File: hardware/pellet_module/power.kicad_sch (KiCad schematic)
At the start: 18 parts, among them J19 Barrel_Jack, U8 MIC5219-3.3YM5, U9 TPS565208

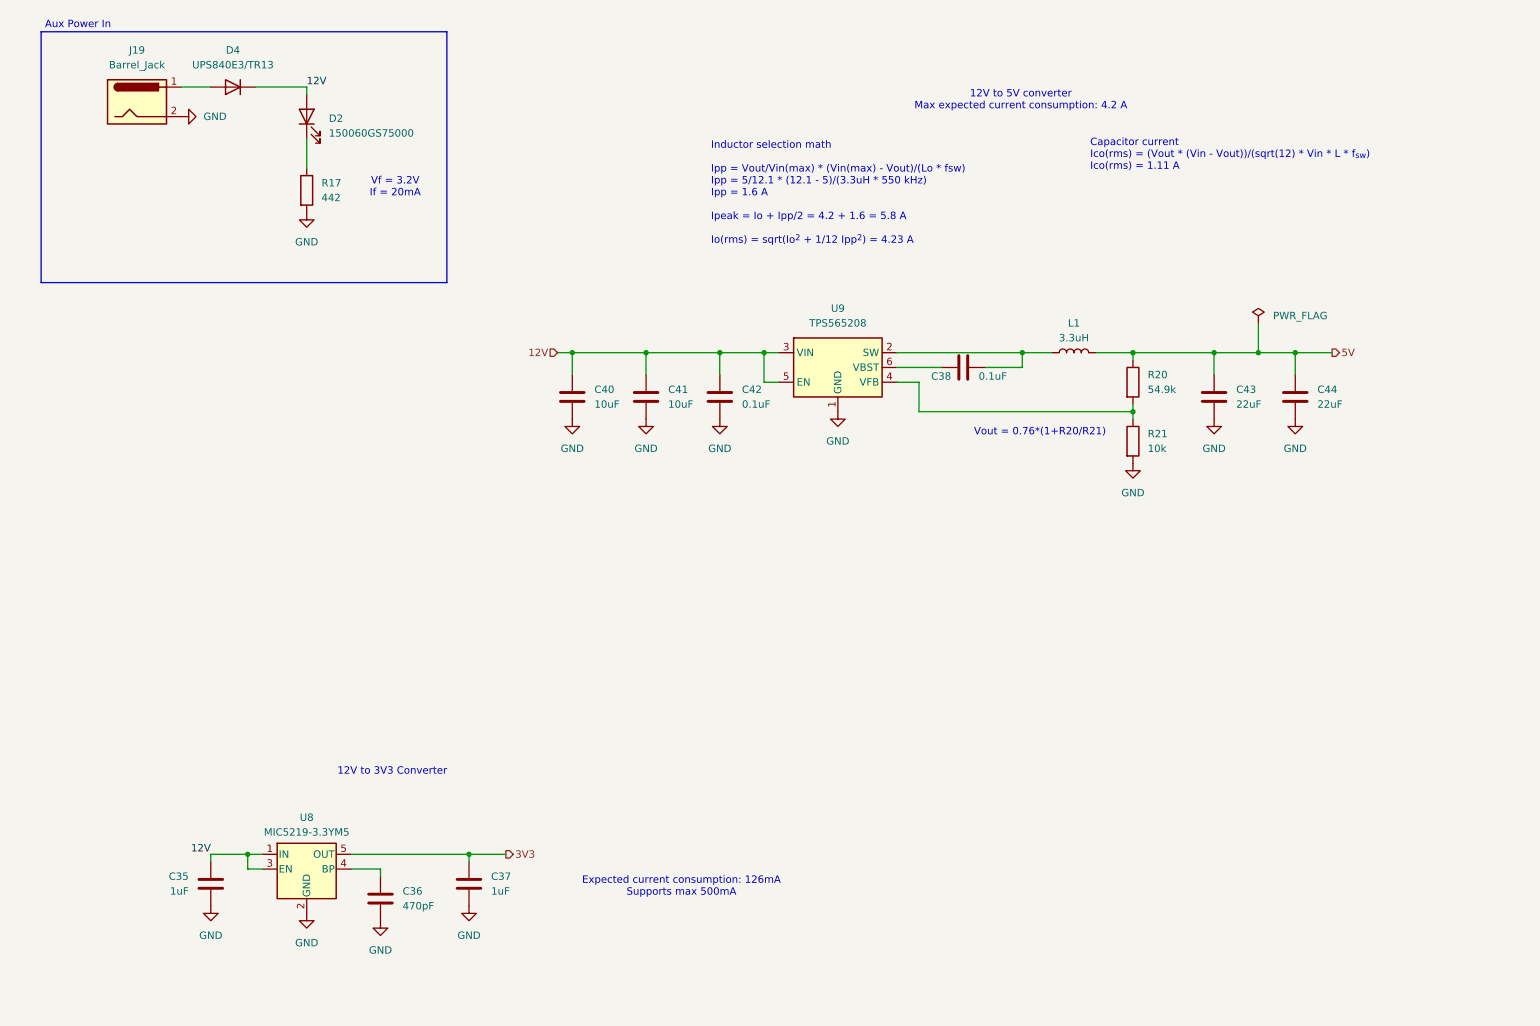
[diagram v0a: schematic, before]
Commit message: add test points, mpns, datasheets
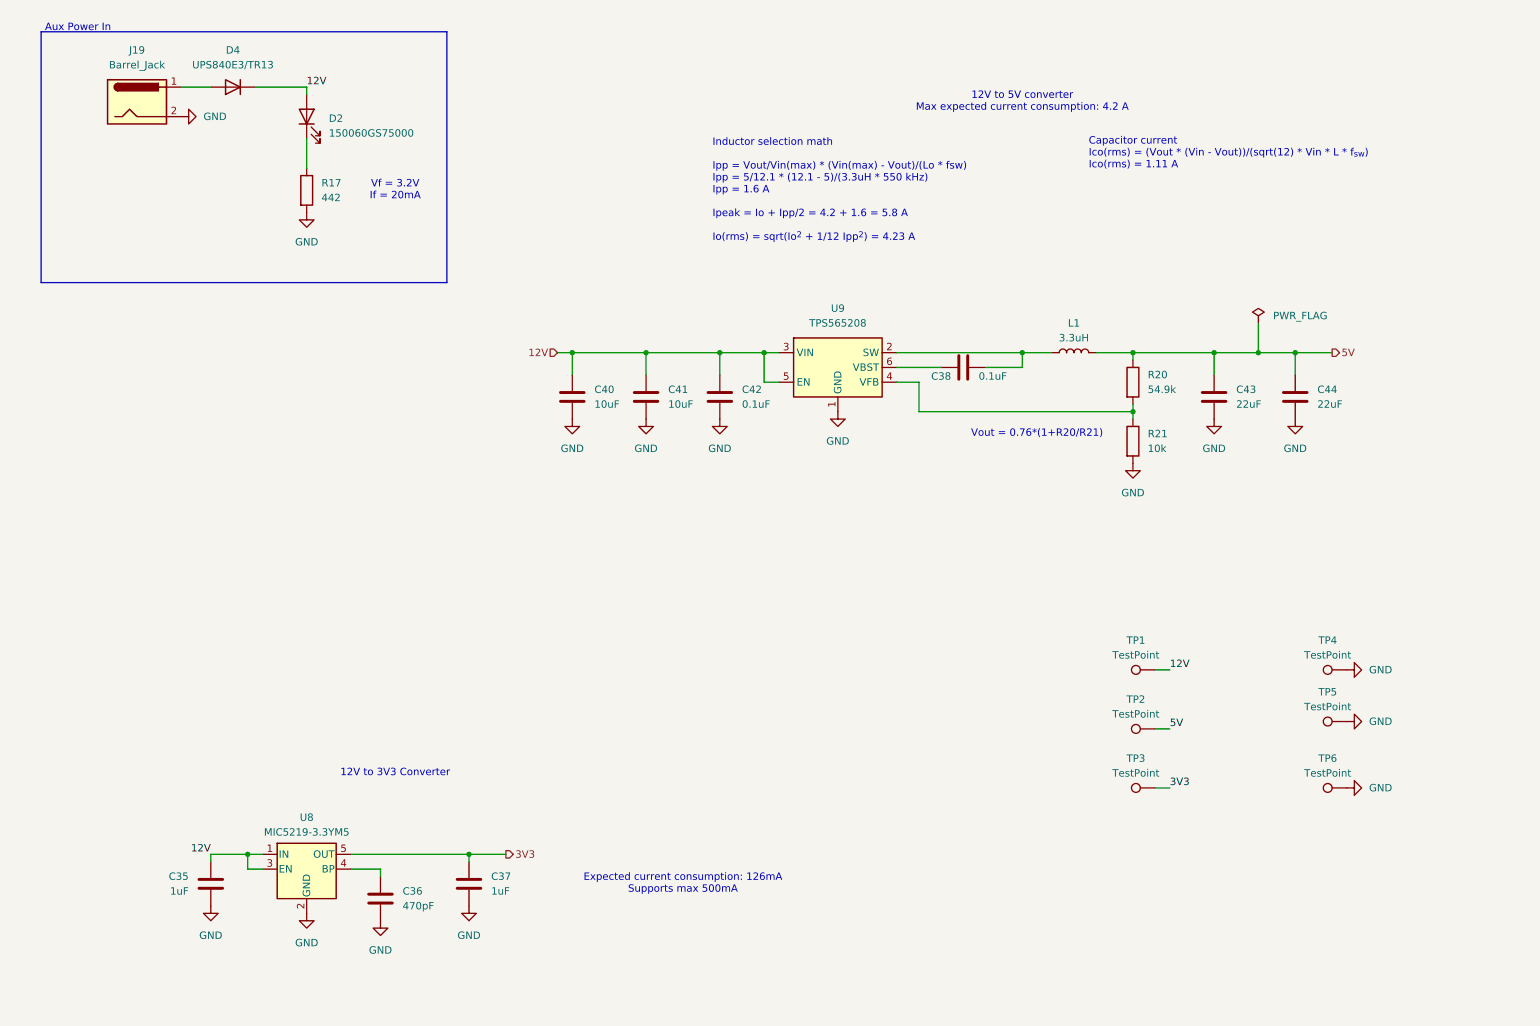
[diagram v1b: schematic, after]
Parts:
- added TP1, TP2, TP3, TP4, TP5, TP6: TestPoint, symbol Connector:TestPoint
- C35, C37: footprint (none) -> Capacitor_SMD:C_0603_1608Metric; MPN (none) -> CC0603KRX7R7BB105
- C36: footprint (none) -> Capacitor_SMD:C_0603_1608Metric; MPN (none) -> CL10C471JB8NNNC
- C38, C42: footprint (none) -> Capacitor_SMD:C_0603_1608Metric; MPN (none) -> CC0603ZRY5V9BB104
- C40, C41: footprint (none) -> Capacitor_SMD:C_0603_1608Metric; MPN (none) -> GRM188R61E106KA73D
- C43, C44: footprint (none) -> Capacitor_SMD:C_0603_1608Metric; MPN (none) -> GRM188R61A226ME15D
- D2: footprint (none) -> Diode_SMD:D_0603_1608Metric; MPN (none) -> 150060GS75000
- D4: footprint (none) -> Diode_SMD:D_Powermite3; MPN (none) -> UPS840E3/TR13
- J19: MPN (none) -> DCJ200-10-A-K1-K
- L1: MPN (none) -> VLS6045EX-3R3N
- R17: MPN (none) -> RC0603FR-07442RL
- R20: MPN (none) -> RC0603FR-0754K9L
- R21: MPN (none) -> RC0603FR-0710KL
- U8: MPN (none) -> MIC5219-3.3YM5
- U9: MPN (none) -> TPS565208
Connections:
- net 12V: now also TP1.1
- net 3V3: now also TP3.1
- net 5V: now also TP2.1
- net GND: now also TP4.1, TP5.1, TP6.1

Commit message: add titles, ESD protection, make changes requested by Ryan
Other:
- company: (none) -> Christie Lab, CU-Anschutz
- title: (none) -> Autotrainer Pellet Module - Power
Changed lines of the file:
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@@
 	(generator_version "8.0")
 	(paper "A4")
+	(title_block
+		(title "Autotrainer Pellet Module - Power")
+		(date "2024-07-09")
+		(rev "v1.0")
+		(company "Christie Lab, CU-Anschutz")
+		(comment 1 "Prepared by LeafLabs, LLC")
+	)
 	(junction
 		(at 134.62 73.66)

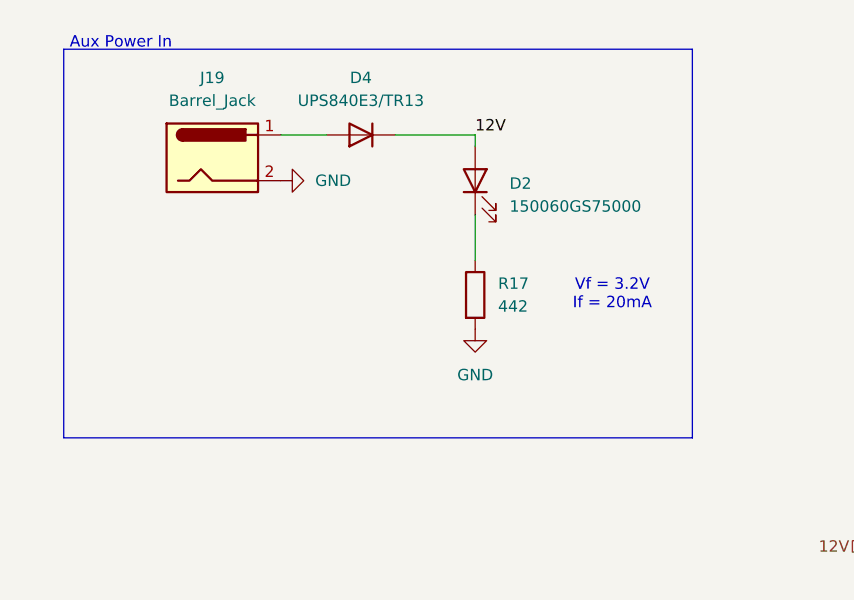
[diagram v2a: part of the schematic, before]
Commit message: * Add footprints for every part * Change power LED from 20mA to 4mA * Edit symbols to match footprints (EPAD -> pin numbers) to eliminate errors on import to pcbnew
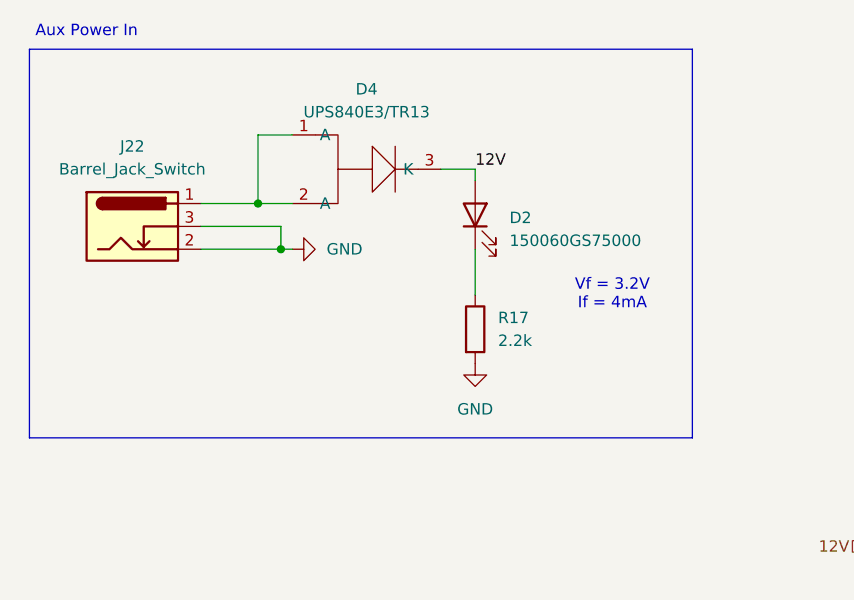
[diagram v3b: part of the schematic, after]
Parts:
- removed J19: Barrel_Jack, symbol Connector:Barrel_Jack
- added J22: Barrel_Jack_Switch, Connector_BarrelJack:BarrelJack_GCT_DCJ200-10-A_Horizontal, symbol Connector:Barrel_Jack_Switch
- D4: symbol Device:D -> Leaf_Diode:Diode_123
- L1: footprint (none) -> Inductor_SMD:L_TDK_VLS6045EX_VLS6045AF
- R17: value 442 -> 2.2k; footprint (none) -> Resistor_SMD:R_0603_1608Metric; MPN RC0603FR-07442RL -> (none)
- R20, R21: footprint (none) -> Resistor_SMD:R_0603_1608Metric
- TP1, TP2, TP3, TP4, TP5, TP6: footprint (none) -> TestPoint:TestPoint_Pad_1.0x1.0mm
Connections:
- net 12V: now also D4.3 (K); no longer D4.1 (K)
- net GND: now also J22.2, J22.3
- net at D4.2 (A): now also D4.1 (A), J22.1
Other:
- note added: "Vf = 3.2V If = 4mA"
- note removed: "Vf = 3.2V If = 20mA"
- moved on the sheet: D2, R17

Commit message: update mechanicals based on dan's comments
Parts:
- D4: footprint Diode_SMD:D_Powermite3 -> Leaf_Diode:POWERMITE3_MCH
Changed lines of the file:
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@@
 			)
 		)
-		(property "Footprint" "Diode_SMD:D_Powermite3"
+		(property "Footprint" "Leaf_Diode:POWERMITE3_MCH"
 			(at 52.07 29.21 0)
 			(effects

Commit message: Releases layout for pellet, magnet, and Jetson breakout boards.
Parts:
- removed U8: MIC5219-3.3YM5, Package_TO_SOT_SMD:SOT-23-5, symbol Regulator_Linear:MIC5219-3.3YM5
- added C49: 10uF, Capacitor_SMD:C_0603_1608Metric, symbol Device:C
- added L2: 3.3uH, Leaf_Inductor:L_Taiyo_Yuden_MAMK, symbol Device:L
- added R27: 33.2k, Resistor_SMD:R_0603_1608Metric, symbol Device:R
- added R28: 10k, Resistor_SMD:R_0603_1608Metric, symbol Device:R
- added U8: TPS561201, Package_TO_SOT_SMD:SOT-23-6, symbol Leaf_Regulator:TPS56120x
- C35: value 1uF -> 0.1uF; LCSC (none) -> C14663; MPN CC0603KRX7R7BB105 -> CC0603KRX7R9BB104
- C36: value 470pF -> 22uF; LCSC (none) -> C59461; MPN CL10C471JB8NNNC -> CL10A226MQ8NRNC
- C37: value 1uF -> 22uF; LCSC (none) -> C59461; MPN CC0603KRX7R7BB105 -> CL10A226MQ8NRNC
- C38, C42: LCSC (none) -> C14663; MPN CC0603ZRY5V9BB104 -> CC0603KRX7R9BB104
- C40, C41: LCSC (none) -> C96446; MPN GRM188R61E106KA73D -> CL10A106MA8NRNC
- C43, C44: LCSC (none) -> C59461; MPN GRM188R61A226ME15D -> CL10A226MQ8NRNC
- D2: LCSC (none) -> C5252984
- D4: LCSC (none) -> C3758317
- J22: LCSC (none) -> C5280493
- L1: LCSC (none) -> C307879
- R17: LCSC (none) -> C4190; MPN (none) -> 0603WAF2201T5E
- R20: LCSC (none) -> C185321
- R21: LCSC (none) -> C25804; MPN RC0603FR-0710KL -> 0603WAF1002T5E
- TP1, TP2, TP3, TP4, TP5, TP6: now left out of the parts list
- U9: LCSC (none) -> C2650336; MPN TPS565208 -> TPS565208DDCR
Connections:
- net 12V: now also C49.1, U8.3 (VIN), U8.5 (EN); no longer C35.1
- net 3V3: now also C36.1, L2.2, R27.1
- net GND: now also C49.2, R28.2, U8.1 (GND); no longer C35.2
- new net: C35.1, U8.6 (VBST)
- new net: C35.2, L2.1, U8.2 (SW)
- new net: R27.2, R28.1, U8.4 (VFB)
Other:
- note added: "Ipp = 3.3/12.1 * (12.1 - 3.3)/(3.3uH * 580kHz) = 1.25 A Ipeak = 0.5 + 1.25/2 = 1.125 A Ilo(rms) = sqrt(0.5^{2}+1/12 Ipp^{2})= 0.62 A"
- note added: "RLC component values suggested in datasheet"
